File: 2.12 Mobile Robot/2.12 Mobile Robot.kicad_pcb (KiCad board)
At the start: 4 copper layers, 176 x 56 mm, 82 parts, among them J1 Motor R, J2 Motor L, J3 GND, J4 Motor Power R, J5 Battery Power, J6 Motor Power L, J7 3.3V, J8 UART, J9 5V, Q1 DMMT5401-7-F, Q2 DMG2305UX-13, SW1 SW_PWR, SW2 RST, SW3 BOOT, SW4 SW_PWR, U1 MOTOR_PWR, U2 ProS3, U3 TCA9548APWR, U4 POWER_IN, U5 TPS564208DDCT

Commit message: Finesse
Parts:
- J1: value Motor R -> Motor Control R
- J2: value Motor L -> Motor Control L
- Q1: footprint footprints:SOT95P285X140-6N -> 2.12_Mobile_Robot:SOT95P285X140-6N
- Q2: footprint footprints:SOT91P240X110-3N -> 2.12_Mobile_Robot:SOT91P240X110-3N
- SW2: value RST -> RST_SW
- SW3: value BOOT -> BOOT_SW
- U1, U4: footprint 2.004:DPAK85P972X240-8N -> 2.12_Mobile_Robot:DPAK85P972X240-8N
- U2: footprint footprints:ProS3_TH -> 2.12_Mobile_Robot:ProS3_TH
- U3: footprint 2.004:SOP65P640X120-24N -> 2.12_Mobile_Robot:SOP65P640X120-24N
- U5: footprint 2.004:SOT95P280X110-6N -> 2.12_Mobile_Robot:SOT95P280X110-6N
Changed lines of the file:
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@@
     )
   )
-  (footprint "2.004:SOT95P280X110-6N" (layer "F.Cu")
+  (footprint "2.12_Mobile_Robot:SOT95P280X110-6N" (layer "F.Cu")
     (at 151.959 134.62)
     (property "MPN" "C2070774")
@@
     (property "Sheetname" "Buck")
     (attr smd)
-    (fp_text reference "U5" (at -0.068 2.347) (layer "F.SilkS")
+    (fp_text reference "U5" (at -0.068 -2.2064) (layer "F.SilkS")
         (effects (font (size 0.64 0.64) (thickness 0.15)))
     )
@@
         (effects (font (size 1 1) (thickness 0.15)))
     )
-    (fp_text value "Motor L" (at -2.794 4.674 180) (layer "F.SilkS")
+    (fp_text value "Motor Control L" (at -2.794 4.674 180) (layer "F.SilkS")
         (effects (font (size 1 1) (thickness 0.15)))
     )
@@
     )
   )
-  (footprint "footprints:SOT95P285X140-6N" (layer "F.Cu")
+  (footprint "2.12_Mobile_Robot:SOT95P285X140-6N" (layer "F.Cu")
     (at 137.735 119.949)
     (property "MANUFACTURER" "Diodes Inc.")
@@
         (effects (font (size 1 1) (thickness 0.15)))
     )
-    (fp_text value "BOOT" (at 3.75 6.7) (layer "F.SilkS")
+    (fp_text value "BOOT_SW" (at 3.75 6.7) (layer "F.SilkS")
         (effects (font (size 1 1) (thickness 0.15)))
     )
@@
     )
   )
-  (footprint "2.004:DPAK85P972X240-8N" (layer "F.Cu")
+  (footprint "2.12_Mobile_Robot:DPAK85P972X240-8N" (layer "F.Cu")
     (at 164.49 113.919 -90)
     (property "Availability" "In Stock")
@@
     (property "ki_description" "Power Switch IC")
     (attr smd)
-    (fp_text reference "U1" (at -2.4775 -5.135 -270) (layer "F.SilkS")
+    (fp_text reference "U1" (at -2.4775 -5.135 -90) (layer "F.SilkS")
         (effects (font (size 1 1) (thickness 0.15)))
     )
-    (fp_text value "MOTOR_PWR" (at -0.0925 0 -270) (layer "F.Fab")
+    (fp_text value "MOTOR_PWR" (at 5.1425 5.135 -90) (layer "F.Fab")
         (effects (font (size 1 1) (thickness 0.15)))
     )
@@
         (effects (font (size 1 1) (thickness 0.15)))
     )
-    (fp_text value "RST" (at 3.75 6.7) (layer "F.SilkS")
+    (fp_text value "RST_SW" (at 3.75 6.7) (layer "F.SilkS")
         (effects (font (size 1 1) (thickness 0.15)))
     )
@@
         (effects (font (size 1 1) (thickness 0.15)))
     )
-    (fp_text value "Motor R" (at -2.921 5.563 180) (layer "F.SilkS")
+    (fp_text value "Motor Control R" (at -2.921 5.563 180) (layer "F.SilkS")
         (effects (font (size 1 1) (thickness 0.15)))
     )
@@
     )
   )
-  (footprint "2.004:DPAK85P972X240-8N" (layer "F.Cu")
+  (footprint "2.12_Mobile_Robot:DPAK85P972X240-8N" (layer "F.Cu")
     (at 164.49 133.0615 -90)
     (property "Availability" "In Stock")
@@
     (property "ki_description" "Power Switch IC")
     (attr smd)
-    (fp_text reference "U4" (at -2.4775 -5.135 90) (layer "F.SilkS")
+    (fp_text reference "U4" (at -2.4775 -5.135 -90) (layer "F.SilkS")
         (effects (font (size 1 1) (thickness 0.15)))
     )
-    (fp_text value "POWER_IN" (at 5.1425 5.135 90) (layer "F.Fab")
+    (fp_text value "POWER_IN" (at 5.1425 5.135 -90) (layer "F.Fab")
         (effects (font (size 1 1) (thickness 0.15)))
     )
@@
     )
   )
-  (footprint "footprints:ProS3_TH" (layer "F.Cu")
+  (footprint "2.12_Mobile_Robot:ProS3_TH" (layer "F.Cu")
     (at 82.809 118.872 180)
     (descr "TH Footprint for the Unexpected Maker ProS3")
@@
     (property "Sheetname" "")
     (attr through_hole)
-    (fp_text reference "U2" (at -0.02 0 180 unlocked) (layer "F.SilkS")
+    (fp_text reference "U2" (at 0 -8.8 180 unlocked) (layer "F.SilkS")
         (effects (font (size 1 1) (thickness 0.15)))
     )
@@
         (effects (font (size 1.6 1.6) (thickness 0.25)))
     )
-    (fp_text user "ANTENNA" (at -4.6 25.6 180 unlocked) (layer "F.Fab")
-        (effects (font (size 0.9 0.9) (thickness 0.1)))
-    )
     (fp_text user "USB" (at 0 -21 180 unlocked) (layer "F.Fab")
         (effects (font (size 1.5 1.5) (thickness 0.3)))
     )
+    (fp_text user "ANTENNA" (at -4.6 25.6 180 unlocked) (layer "F.Fab")
+        (effects (font (size 0.9 0.9) (thickness 0.1)))
+    )
     (fp_line (start -8.91 27.7622) (end -8.91 -24.13)
       (stroke (width 0.05) (type solid)) (layer "F.Fab"))
@@
     )
   )
-  (footprint "footprints:SOT91P240X110-3N" (layer "F.Cu")
+  (footprint "2.12_Mobile_Robot:SOT91P240X110-3N" (layer "F.Cu")
     (at 141.8505 119.949 180)
     (property "MANUFACTURER" "Diodes Inc.")
@@
     (property "Sheetname" "ZVD")
     (attr smd)
-    (fp_text reference "Q2" (at -0.13 -2.548) (layer "F.SilkS")
+    (fp_text reference "Q2" (at -0.13 -2.548 180) (layer "F.SilkS")
         (effects (font (size 0.8 0.8) (thickness 0.15)))
     )
-    (fp_text value "DMG2305UX-13" (at 5.458 2.548) (layer "F.Fab")
+    (fp_text value "DMG2305UX-13" (at 5.458 2.548 180) (layer "F.Fab")
         (effects (font (size 0.8 0.8) (thickness 0.15)))
     )
@@
     )
   )
-  (footprint "2.004:SOP65P640X120-24N" (layer "F.Cu")
+  (footprint "2.12_Mobile_Robot:SOP65P640X120-24N" (layer "F.Cu")
     (at 59.207 108.077 90)
     (property "MPN" "C130026")

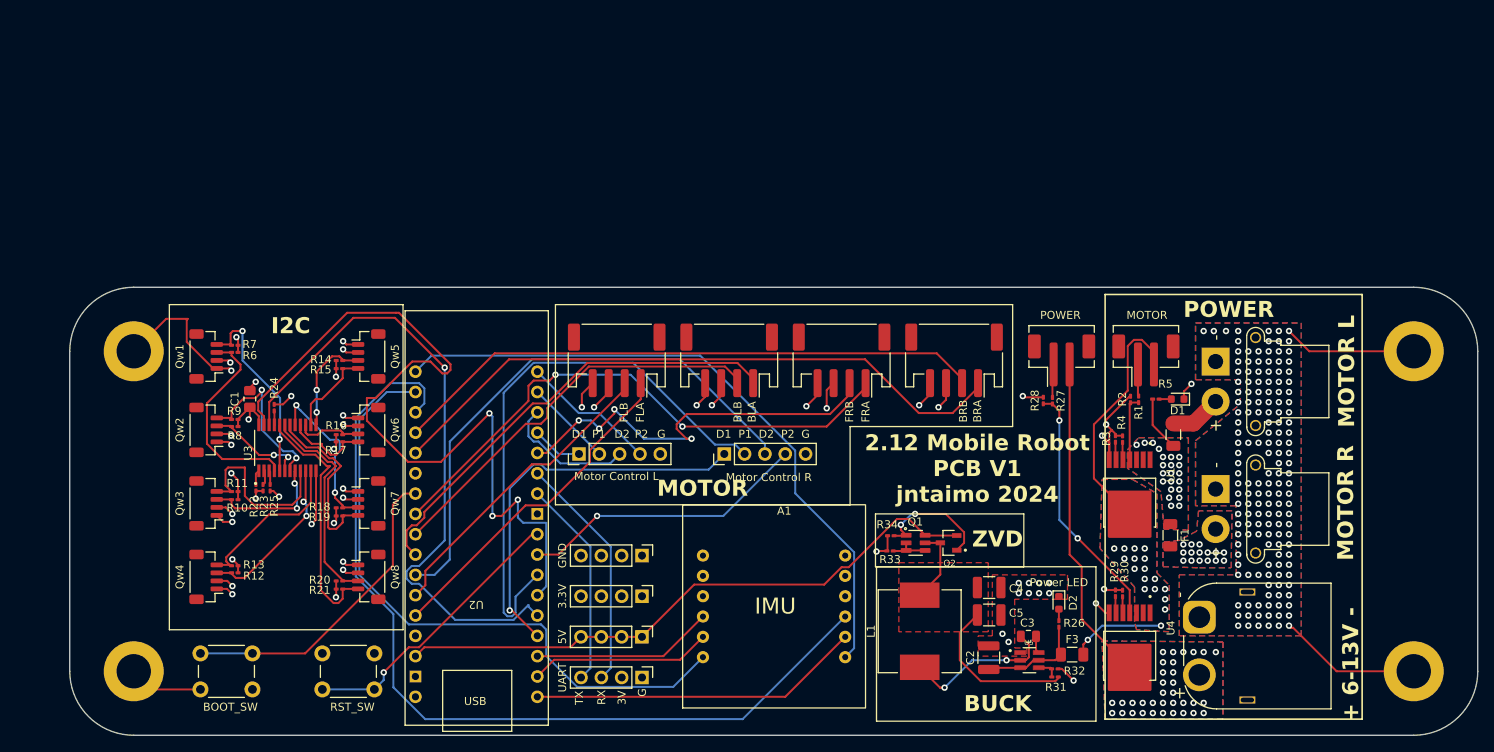
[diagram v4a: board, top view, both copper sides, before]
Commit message: Added silkscreen callouts and fixed resistors
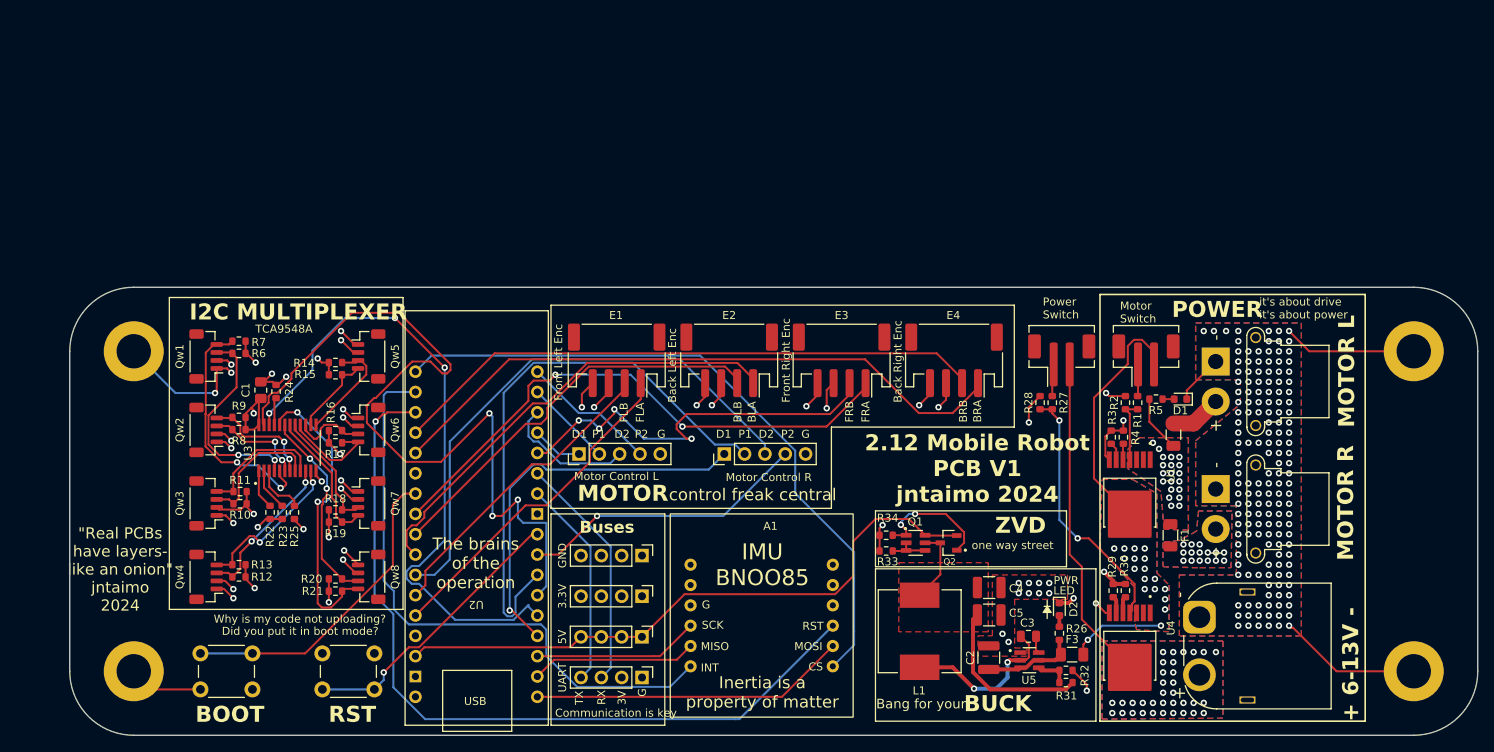
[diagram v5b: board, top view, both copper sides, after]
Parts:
- removed ? (x3): , 
- added REF**: MountingHole_4.3mm_M4_DIN965_Pad, MountingHole:MountingHole_4.3mm_M4_DIN965_Pad, F.Cu at (200.0, 96.0)
- added REF**: MountingHole_4.3mm_M4_DIN965_Pad, MountingHole:MountingHole_4.3mm_M4_DIN965_Pad, F.Cu at (200.0, 136.0)
- added REF**: MountingHole_4.3mm_M4_DIN965_Pad, MountingHole:MountingHole_4.3mm_M4_DIN965_Pad, F.Cu at (40.0, 136.0)
- D2: value Power LED -> PWR
- R1, R10, R11, R12, R13, R14, R15, R16, R17, R18, R19, R2, R20, R21, R22, R23, R24, R25, R26, R27, R28, R29, R3, R30, R31, R32, R33, R34, R4, R5, R6, R7, R8, R9: footprint Resistor_SMD:R_0201_0603Metric_Pad0.64x0.40mm_HandSolder -> Resistor_SMD:R_0603_1608Metric
- moved R25 4.33 mm to (60.1, 116.1)
- moved R23 3.91 mm to (58.6, 116.1)
- moved R22 3.55 mm to (57.0, 116.1)
- moved R24 2.03 mm to (57.8, 101.0)
- moved A1 1.93 mm to (119.8, 117.6)
- moved C1 1.76 mm to (55.9, 100.9)
- moved R31 1.54 mm to (156.5, 137.4)
- moved R32 1.41 mm to (156.5, 135.9)
- moved R26 1.17 mm to (155.7, 131.3)
- moved R15 0.91 mm to (65.2, 98.9)
- moved R19 0.91 mm to (65.2, 117.3)
- moved R10 0.83 mm to (53.3, 115.1)
- moved D2 0.80 mm to (155.7, 128.2)
- moved R2 0.75 mm to (164.0, 102.4)
- moved R12 0.73 mm to (53.1, 124.2)
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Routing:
- net +3.3V: track 54.5 -> 70.5 mm, vias 21 -> 20
- net /IMU_RST: track 113.2 -> 101.1 mm, vias 0 -> 1
- net /Qwiic/SC1: track 20.9 -> 14.2 mm
- net /Qwiic/SC2: track 22.0 -> 16.1 mm
- net /Qwiic/SC0: track 24.5 -> 30.1 mm
- net /Qwiic/SD6: track 20.8 -> 15.3 mm, vias 2 -> 0
- net /Qwiic/SC7: track 31.6 -> 36.9 mm, vias 0 -> 2
- net /Qwiic/SC6: track 22.3 -> 17.2 mm
- net Net-(U3-~{RESET}): track 1.75 -> 6.49 mm
- net /IMU_INT: track 80.1 -> 75.5 mm
- net GND: track 133.3 -> 137.1 mm, vias 189 -> 190
- net Net-(U3-A1): track 1.89 -> 5.31 mm
- net Net-(U3-A0): track 1.85 -> 4.95 mm
- net +5V: track 75.6 -> 78.2 mm
- net /SCK: track 22.8 -> 20.7 mm
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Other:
- board text added: "BOOT"
- board text added: "Back Left Enc"
- board text added: "Back Right Enc"
- board text added: "Bang for your"
- board text added: "Buses"
- board text added: "CS"
- board text added: "Communication is key"
- board text added: "Did you put it in boot mode?"
- board text added: "Front Left Enc"
- board text added: "Front Right Enc"
- board text added: "I2C MULTIPLEXER"
- board text added: "IMU BNOO85"
- board text added: "INT"
- board text added: "Inertia is a property of matter"
- board text added: "LED"
- board text added: "MISO"
- board text added: "MOSI"
- board text added: "Motor Switch"
- board text added: "Power Switch"
- board text added: "RST"
- board text added: "SCK"
- board text added: "TCA9548A"
- board text added: "The brains of the operation"
- board text added: "Why is my code not uploading?"
- board text added: "control freak central"
- board text added: "it's about drive it's about power"
- board text added: "one way street"
- board text added: "{dblquote}Real PCBs have layers- like an onion{dblquote} jntaimo 2024"
- board text removed: "I2C"
- board text removed: "IMU"
